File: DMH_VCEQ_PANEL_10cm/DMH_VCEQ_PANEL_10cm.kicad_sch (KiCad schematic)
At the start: 36 parts, among them J0 Panel_GND_Solder_Wire_Pad

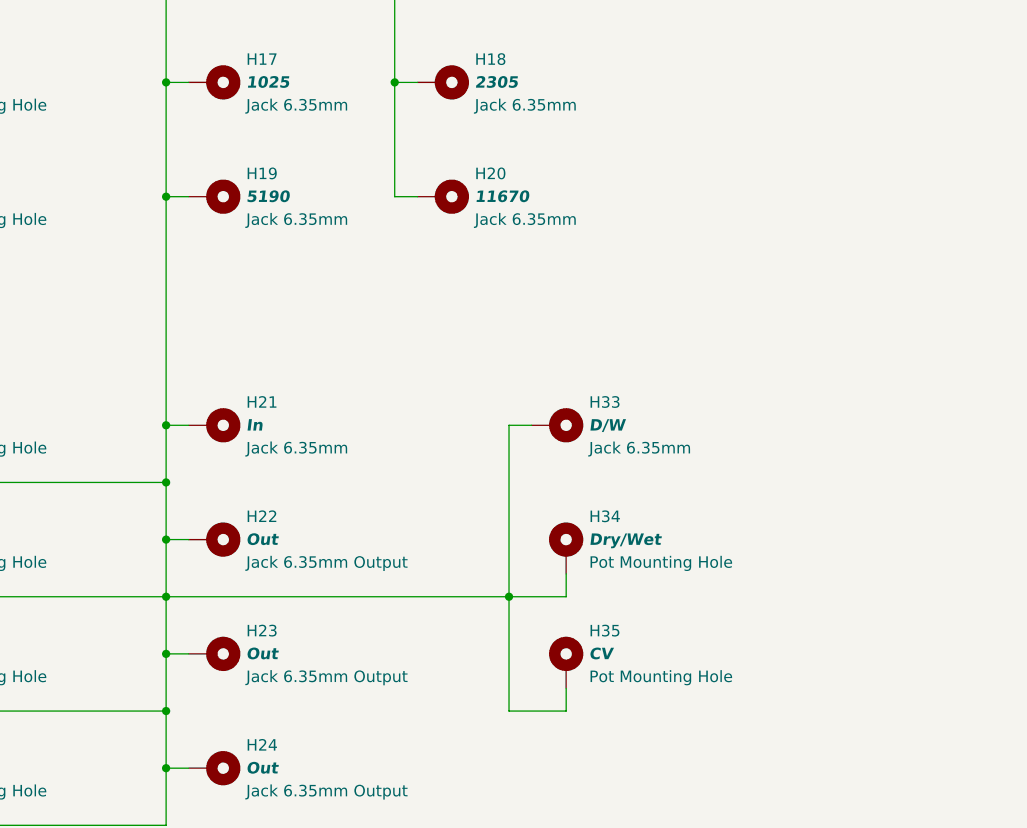
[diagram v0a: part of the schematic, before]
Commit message: Designed 10cm panel
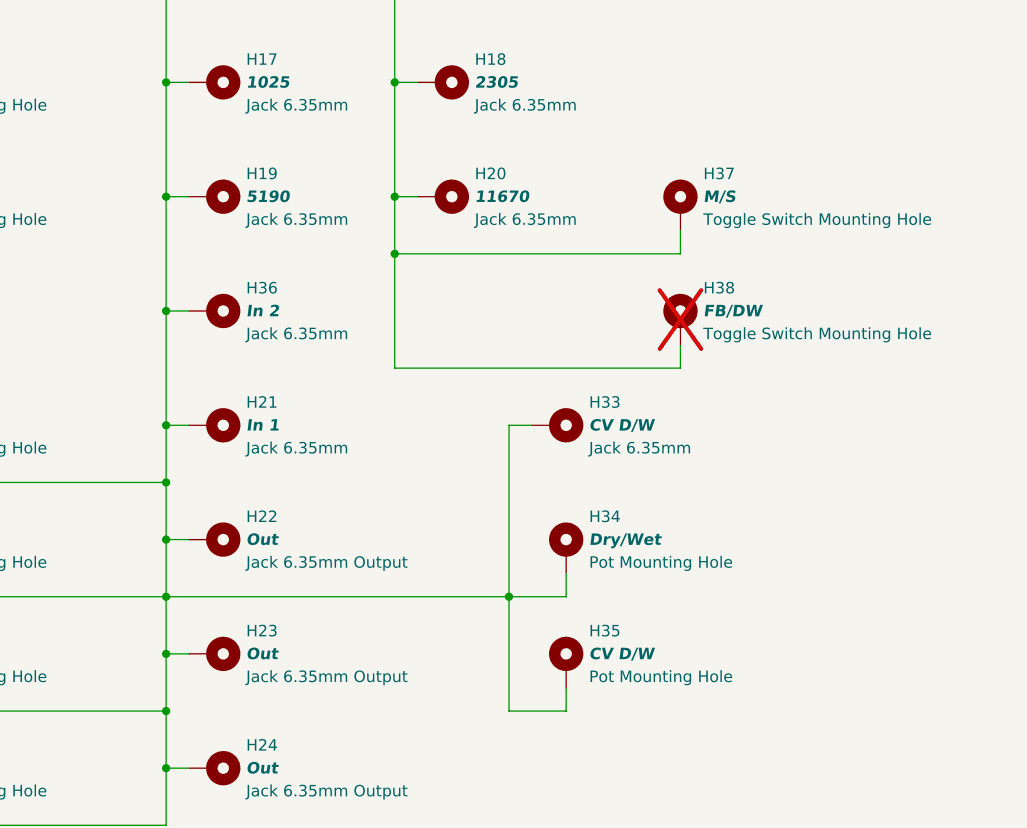
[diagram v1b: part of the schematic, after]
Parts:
- added H36: In 2, SynthStuff:Jack_6.35mm_Cutout_v3, symbol SynthStuff:MountingHole_Jack6.35mm_v2
- added H37: M/S, SynthStuff:Toggle_Switch_TE_Cutout, symbol SynthStuff:MountingHole_ToggleSwitch
- added H38: FB/DW, SynthStuff:Toggle_Switch_TE_Cutout, symbol SynthStuff:MountingHole_ToggleSwitch
- H21: value In -> In 1
- H33: value D/W -> CV D/W
- H35: value CV -> CV D/W
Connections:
- net GND: now also H36.1, H37.1, H38.1

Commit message: Improving 10cm version
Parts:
- removed H22: Out, SynthStuff:Jack_6.35mm_Cutout_Output_v6, symbol SynthStuff:MountingHole_Jack6.35mm_Output_v2
- removed H33: CV D/W, SynthStuff:Jack_6.35mm_Cutout_v3, symbol SynthStuff:MountingHole_Jack6.35mm_v2
- added H22: Dry/Wet, SynthStuff:Jack_6.35mm_Cutout_v3, symbol SynthStuff:MountingHole_Jack6.35mm_v2
- added H33: Out, SynthStuff:Jack_6.35mm_Cutout_Output_v6, symbol SynthStuff:MountingHole_Jack6.35mm_Output_v2
- added H39: FB, SynthStuff:Jack_6.35mm_Cutout_v3, symbol SynthStuff:MountingHole_Jack6.35mm_v2
- H34: value Dry/Wet -> In 2 [FB]; footprint SynthStuff:Pot_Cutout_Tiny_text_P110KH1 -> SynthStuff:Pot_Cutout_Tiny
- H35: value CV D/W -> In 1; footprint SynthStuff:Pot_Cutout_Tiny_attv_P110KH1 -> SynthStuff:Pot_Cutout_Tiny
- H37: now not fitted
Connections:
- net GND: now also H22.1, H33.1, H39.1
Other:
- note added: "Out jack Tip goes to Tip Noramlled of In 2, SO In 2 gain is normally a Feedback knob unless something is connected to jack In 2"
